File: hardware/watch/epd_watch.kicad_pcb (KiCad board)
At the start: 4 copper layers, 35 x 37 mm, 56 parts, among them J1 SWD_interface, J2 sound_connector, P1 FPC, Q1 Si1308EDL, SW1 BTN_UP, SW2 BTN_MIDDLE, SW3 BTN_DOWN, U1 nRF52832-QFxx, U2 XC6206PxxxMR, U3 TP4057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

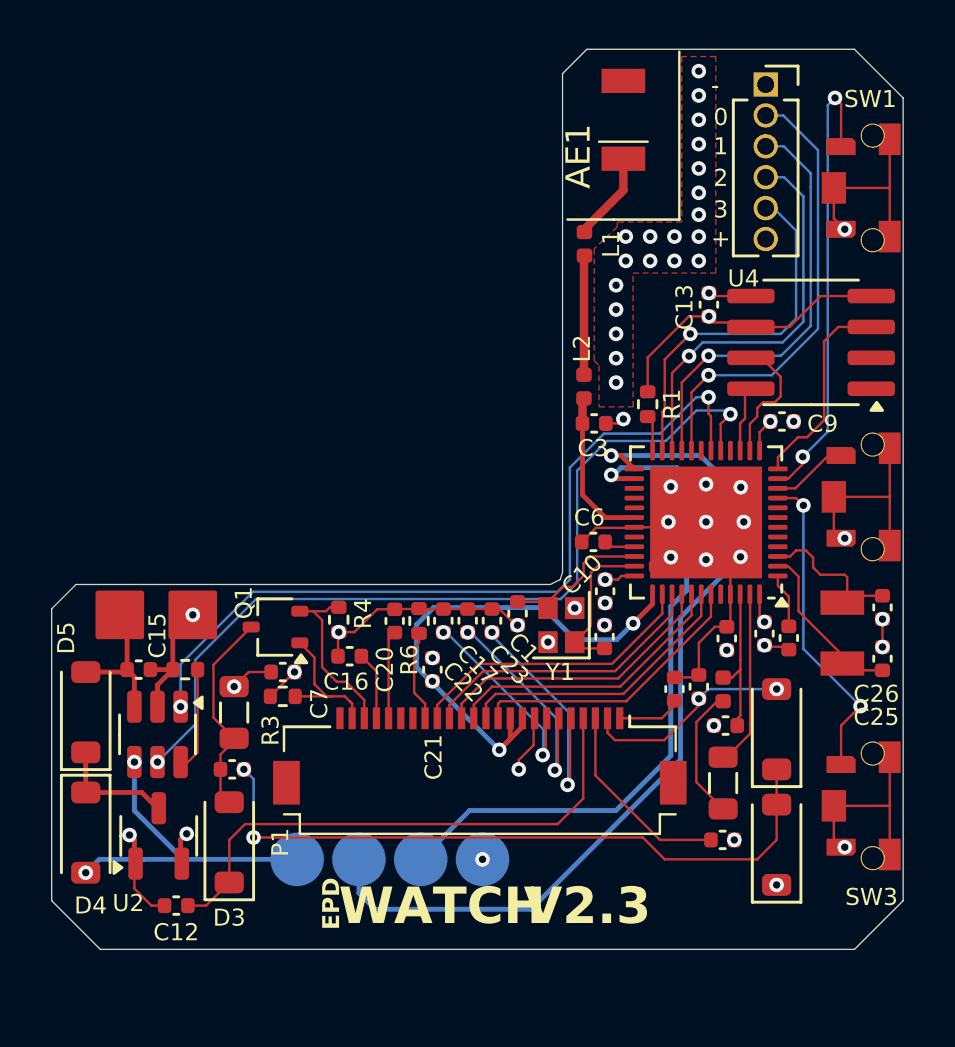
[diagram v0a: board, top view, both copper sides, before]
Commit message: didnt read datasheet well enough
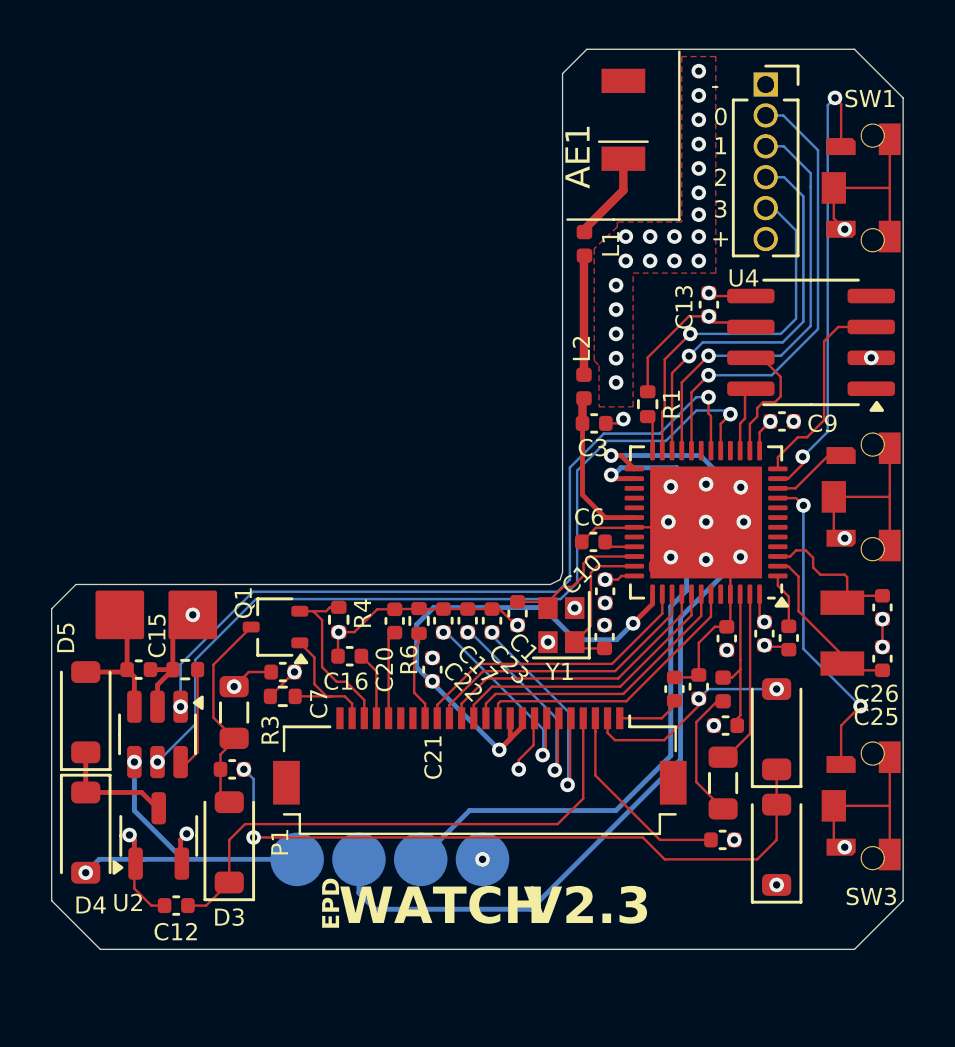
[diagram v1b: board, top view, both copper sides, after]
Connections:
- U4 pad 2: unconnected-(U4-VCC-Pad2) -> GND
- U4 pad 4: 3.3V -> unconnected-(U4-~{RST}-Pad4)
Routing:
- net 3.3V: track 18.8 -> 13.4 mm
- net GND: vias 53 -> 54
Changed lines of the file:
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@@
 	(net 63 "Net-(U1-P0.01{slash}XL2)")
 	(net 64 "unconnected-(U4-32KHZ-Pad1)")
-	(net 65 "unconnected-(U4-VCC-Pad2)")
+	(net 65 "unconnected-(U4-~{RST}-Pad4)")
 	(net 66 "CHRG")
 	(net 67 "STDBY")
@@
 			(layers "F.Cu" "F.Paste" "F.Mask")
 			(roundrect_rratio 0.25)
-			(net 65 "unconnected-(U4-VCC-Pad2)")
+			(net 4 "GND")
 			(pinfunction "VCC")
-			(pintype "power_in+no_connect")
+			(pintype "power_in")
 		)
 		(pad "3" smd roundrect
@@
 			(layers "F.Cu" "F.Paste" "F.Mask")
 			(roundrect_rratio 0.25)
-			(net 11 "3.3V")
+			(net 65 "unconnected-(U4-~{RST}-Pad4)")
 			(pinfunction "~{RST}")
 			(pintype "bidirectional")
@@
 	)
 	(via
+		(at 165.19 97.685)
+		(size 0.6)
+		(drill 0.3)
+		(layers "F.Cu" "B.Cu")
+		(net 4)
+	)
+	(via
 		(at 156.95 102.98)
 		(size 0.6)
@@
 	)
 	(segment
-		(start 161.835 96.415)
-		(end 163.105 95.145)
-		(width 0.1)
-		(layer "F.Cu")
-		(net 11)
-	)
-	(segment
 		(start 160.6 108.39)
 		(end 160.75 108.54)
@@
 	)
 	(segment
-		(start 163.105 95.145)
-		(end 165.19 95.145)
-		(width 0.1)
-		(layer "F.Cu")
-		(net 11)
-	)
-	(segment
 		(start 157.692182 95.98)
 		(end 158.515 95.98)
@@
 	)
 	(segment
-		(start 160.24 96.415)
-		(end 161.835 96.415)
-		(width 0.1)
-		(layer "F.Cu")
-		(net 11)
-	)
-	(segment
 		(start 139.6 110.6)
 		(end 139 111.2)
@@
 		(width 0.1)
 		(layer "F.Cu")
-		(net 40)
-	)
-	(segment
-		(start 143.75 111.8)
-		(end 143.85 111.9)
-		(width 0.1)
-		(layer "F.Cu")

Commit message: first start at fixing battery measurement and lowering power consumption
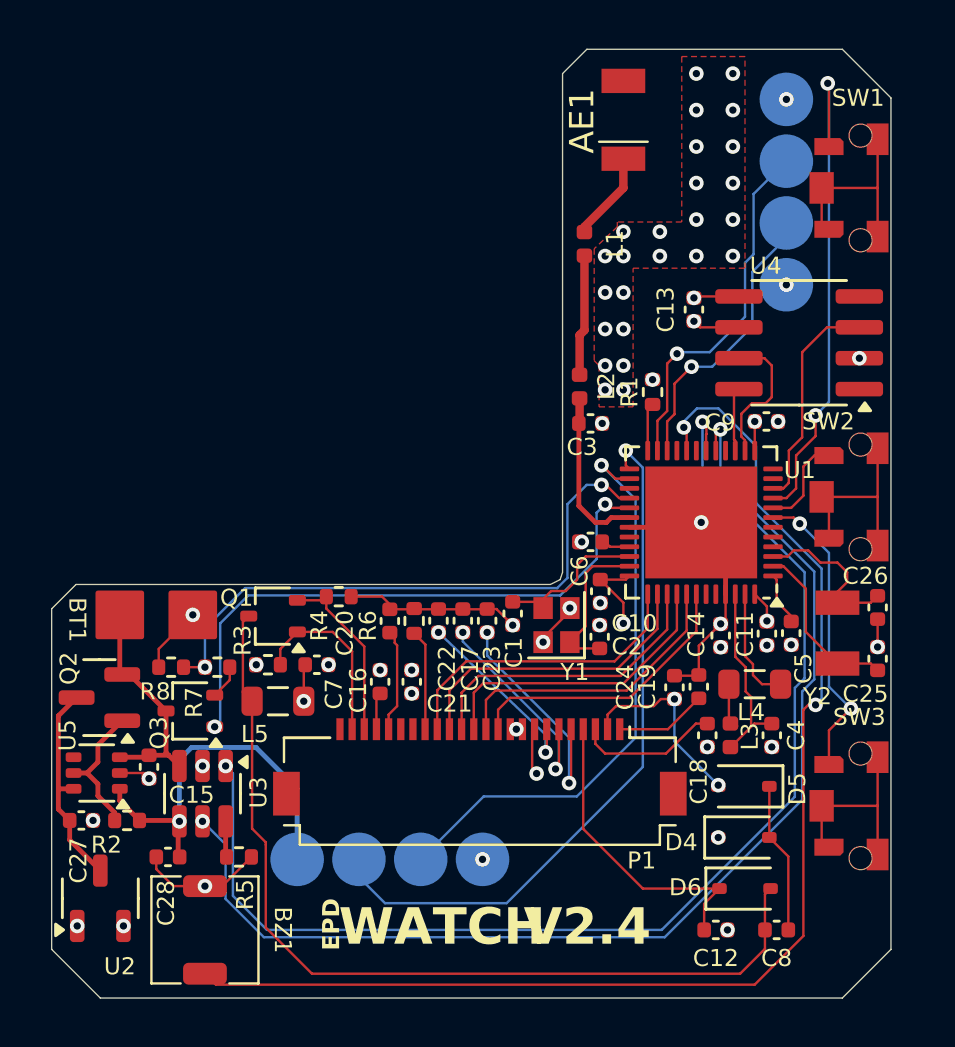
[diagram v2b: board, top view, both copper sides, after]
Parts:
- removed D1, D2, D3: MBR0530, Diode_SMD:D_SOD-123
- added BZ1: FUET-4020, epd_watch:FUET-4020, F.Cu at (137.8, 121.2)
- added C27: 4.7uF, Capacitor_SMD:C_0402_1005Metric, F.Cu at (132.7, 116.7)
- added C28: 4.7uF, Capacitor_SMD:C_0402_1005Metric, F.Cu at (136.3, 118.2)
- added D6: 1N5819WS, Diode_SMD:D_SOD-323, F.Cu at (160.0, 119.5)
- added Q2: AO3401A, Package_TO_SOT_SMD:SOT-23, F.Cu at (133.5, 111.7)
- added Q3: Si1308EDL, Package_TO_SOT_SMD:SOT-323_SC-70, F.Cu at (137.2, 112.2)
- added R2: 10K, Resistor_SMD:R_0402_1005Metric, F.Cu at (134.6, 116.7)
- added R7: 10K, Resistor_SMD:R_0402_1005Metric, F.Cu at (138.3, 110.4)
- added R8: 10K, Resistor_SMD:R_0402_1005Metric, F.Cu at (136.4, 110.4)
- added U5: LM66100DCK, Package_TO_SOT_SMD:SOT-363_SC-70-6, F.Cu at (133.3, 114.8)
- D4, D5: value MBR0530 -> 1N5819WS; footprint Diode_SMD:D_SOD-123 -> Diode_SMD:D_SOD-323
- J2: value sound_connector -> GPIO; footprint Connector_PinSocket_1.27mm:PinSocket_1x06_P1.27mm_Vertical -> epd_watch:pogo_conn; moved to B.Cu
- moved D5 27.5 mm to (159.9, 117.4), turned to 0 degrees
- moved D4 27.1 mm to (159.9, 115.3), turned to 180 degrees
- moved C8 23.3 mm to (161.3, 121.2)
- moved C12 22.2 mm to (158.8, 121.2), turned to 180 degrees
- moved R5 8.01 mm to (139.2, 118.2), turned to 0 degrees
- moved J2 4.50 mm to (161.7, 90.9), turned to 90 degrees
- moved C18 4.35 mm to (158.4, 113.2), turned to -90 degrees
- moved L4 4.27 mm to (160.4, 111.1), turned to 0 degrees
- moved C15 4.02 mm to (135.5, 114.5), turned to 90 degrees
- moved U2 3.51 mm to (133.5, 119.9)
- moved U3 3.06 mm to (137.7, 115.6)
- moved C4 1.94 mm to (161.1, 113.2), turned to 90 degrees
- moved L3 1.91 mm to (159.4, 113.2), turned to 90 degrees
- moved L5 1.86 mm to (140.8, 111.8), turned to 180 degrees
- moved C16 1.63 mm to (145.0, 111.0), turned to 90 degrees
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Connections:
- BT1 pad 1: Net-(BT1-+) -> VBAT
- C15 pad 2: Net-(BT1-+) -> VBAT
- C21 pad 1: EPD_3.3V -> 3.3V
- C8 pad 1: Net-(D1-K) -> Net-(D4-K)
- D4 pad 2: VBUS -> PREVGL
- D5 pad 1: Net-(D4-K) -> GND
- D5 pad 2: Net-(BT1-+) -> Net-(D4-K)
- J2 pad 1: GND -> 3.3V
- J2 pad 2: SND_0 -> GPIO_0
- J2 pad 3: SND_1 -> GPIO_1
- J2 pad 4: SND_2 -> GND
- P1 pad 15: EPD_3.3V -> 3.3V
- P1 pad 16: EPD_3.3V -> 3.3V
- U1 pad 10: BTN_MIDDLE -> SQW
- U1 pad 11: BTN_UP -> unconnected-(U1-NFC1/P0.09-Pad11)
- U1 pad 12: SQW -> unconnected-(U1-NFC2/P0.10-Pad12)
- U1 pad 20: SND_0 -> BUZZER
- U1 pad 21: SND_1 -> unconnected-(U1-P0.18/SWO-Pad21)
- U1 pad 22: SND_2 -> GPIO_0
- U1 pad 23: SND_3 -> GPIO_1
- U1 pad 28: unconnected-(U1-P0.23-Pad28) -> BAT_LVL
- U1 pad 29: unconnected-(U1-P0.24-Pad29) -> BAT_LVL_EN
- U1 pad 37: EPD_3.3V -> BUSY
- U1 pad 38: BUSY -> RES
- U1 pad 39: RES -> DC
- U1 pad 40: DC -> CS
- U1 pad 41: CS -> SCK
- U1 pad 42: SCK -> MOSI
- U1 pad 43: MOSI -> unconnected-(U1-P0.31/AIN7-Pad43)
- U1 pad 7: unconnected-(U1-P0.05/AIN3-Pad7) -> BTN_DOWN
- U1 pad 8: unconnected-(U1-P0.06-Pad8) -> BTN_MIDDLE
- U1 pad 9: BTN_DOWN -> BTN_UP
- U2 pad 3: Net-(D4-K) -> Net-(Q2-D)
- U3 pad 3: Net-(BT1-+) -> VBAT
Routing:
- net BUZZER: track 0.00 -> 52.4 mm, vias 0 -> 2
- net Net-(D6-A): track 8.62 -> 37.6 mm
- net Net-(D1-K): track 28.1 -> 0.00 mm, vias 2 -> 0
- net BAT_LVL: track 0.00 -> 24.4 mm, vias 0 -> 2
- net BAT_LVL_EN: track 0.00 -> 24.4 mm, vias 0 -> 2
- net EPD_3.3V: track 21.3 -> 0.00 mm, vias 3 -> 0
- net SND_0: track 18.8 -> 0.00 mm, vias 1 -> 0
- net SND_1: track 17.6 -> 0.00 mm, vias 1 -> 0
- net CHRG: track 32.9 -> 50.0 mm
- net SND_2: track 16.5 -> 0.00 mm, vias 1 -> 0
- net SND_3: track 15.2 -> 0.00 mm, vias 1 -> 0
- net GPIO_1: track 0.00 -> 14.8 mm, vias 0 -> 1
- net STDBY: track 35.5 -> 48.3 mm
- net GPIO_0: track 0.00 -> 11.9 mm, vias 0 -> 1
- net PREVGH: track 22.4 -> 12.7 mm
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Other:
- board size 35 x 37 mm -> 34.5 x 39 mm
- board text added: "V2.4"
- board text removed: "+"
- board text removed: "-"
- board text removed: "0"
- board text removed: "1"
- board text removed: "2"
- board text removed: "3"
- board text removed: "V2.3"

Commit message: finalized V2.4
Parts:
- removed J2: GPIO, epd_watch:pogo_conn
- added GPIO: GPIO, epd_watch:gpio_conn, B.Cu at (162.6, 91.6)
- C4: value 1.0uF -> 1.0uF/50V
- moved L5 21.6 mm to (160.1, 121.4), turned to 0 degrees
- moved R7 1.90 mm to (136.4, 110.3), turned to 0 degrees
- moved R8 1.90 mm to (138.3, 110.3), turned to 0 degrees
- moved C12 1.50 mm to (157.8, 120.1), turned to 90 degrees
- moved C8 1.45 mm to (162.5, 120.4), turned to -90 degrees
- moved C16 0.30 mm to (144.7, 111.0)
- moved C21 0.30 mm to (146.0, 111.0)
- moved C9 0.30 mm to (161.2, 100.3)
- moved P1 0.30 mm to (148.8, 115.7)
- moved R1 0.20 mm to (156.0, 99.1)
- renumbered J1 to CHARGER/SWD
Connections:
- Q3 pad 2: Net-(Q3-S) -> GND
- Q3 pad 3: VBAT -> Net-(Q3-D)
- R7 pad 1: Net-(Q3-S) -> VBAT
- R8 pad 2: GND -> Net-(Q3-D)
- U1 pad 19: unconnected-(U1-P0.16-Pad19) -> BUZZER
- U1 pad 20: BUZZER -> GPIO_0
- U1 pad 21: unconnected-(U1-P0.18/SWO-Pad21) -> GPIO_1
- U1 pad 22: GPIO_0 -> GPIO_2
- U1 pad 23: GPIO_1 -> GPIO_3
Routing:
- net GPIO_3: track 0.00 -> 16.8 mm, vias 0 -> 1
- net GPIO_2: track 0.00 -> 14.5 mm, vias 0 -> 1
- net GND: track 59.4 -> 48.9 mm, vias 57 -> 69
- net BUZZER: track 52.4 -> 56.0 mm
- net Net-(Q3-D): track 0.00 -> 3.41 mm
- net GPIO_1: track 14.8 -> 12.1 mm
- net PREVGH: track 12.7 -> 10.8 mm
- net Net-(D6-A): track 37.6 -> 39.2 mm
- net GPIO_0: track 11.9 -> 10.4 mm
- net Net-(Q3-S): track 1.41 -> 0.00 mm
- net SWDCLK: track 29.3 -> 30.5 mm
- net VBAT: track 9.44 -> 10.6 mm
- net Net-(D4-K): track 6.22 -> 5.22 mm
- net SWDIO: track 24.1 -> 24.7 mm
- net STDBY: track 48.3 -> 48.8 mm
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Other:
- board text added: "+"
- board text added: "-"
- board text added: "0"
- board text added: "1"
- board text added: "2"
- board text added: "3"
